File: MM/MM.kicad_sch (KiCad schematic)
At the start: 51 parts, among them J1 USB_C_Receptacle_PowerOnly_6P, J2 Conn_02x16_Odd_Even, SW1 C2890358, SW2 C2890358, U1 DRV8833PWPR, U2 DRV8833PWPR, U3 TP5100, U4 INA219AxD, U5 XL1509-3.3, U6 IP2721, U7 TPS2042D, U8 XL1509-5.0

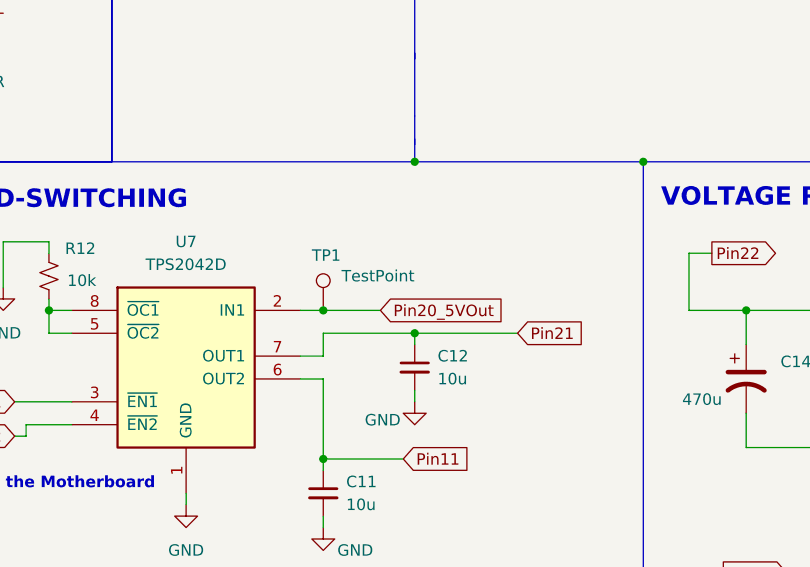
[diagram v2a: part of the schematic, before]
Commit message: Updated voltage regulation, INA219, USB-C, and load-switching circuits. Added verified footprints for 470uF SMD capacitor (C_Elec_8x10.2), IP2721, TPS2042D, and XL1509 regulators. Verified component dimensions and corrected capacitor footprints for JLCPCB compatibility.
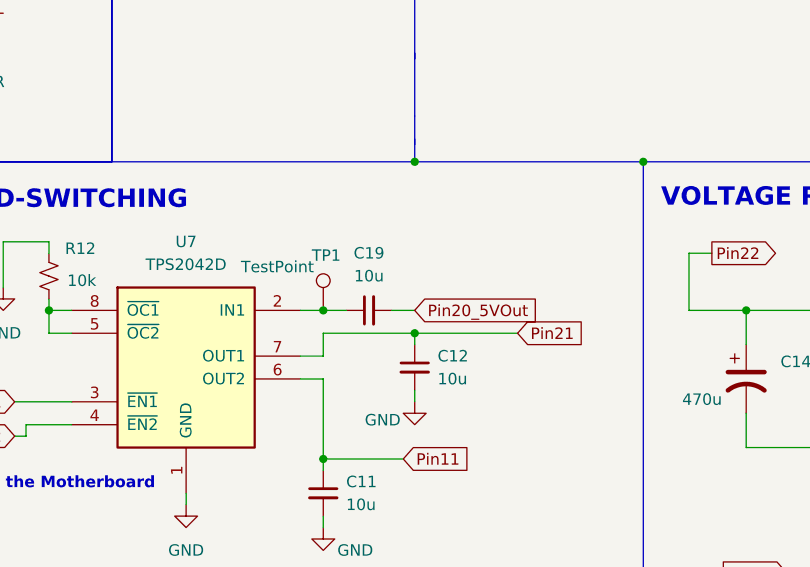
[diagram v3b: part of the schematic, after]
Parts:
- added C19: 10u, CL21A106KAYNNNE:CAPC2012X135N, symbol Device:C_Small
- C10, C11, C12, C9: footprint (none) -> CL21A106KAYNNNE:CAPC2012X135N; LSCS (none) -> C15850
- C14, C16: footprint (none) -> Capacitor_SMD:C_Elec_8x10.2; LSCS (none) -> C3341
- C7, C8: footprint (none) -> CL31B105KBHNNNE:CAPC3216X180N; LSCS (none) -> C1848
- L2: LSCS (none) -> C3341
- R10, R11: footprint (none) -> 0603WAF3301T5E:RESC1608X55N; LSCS (none) -> C22978
- R12, R3, R9: footprint (none) -> 0603WAF1002T5E:RESC1608X55N; LSCS (none) -> C25804
- R5: footprint (none) -> WSL25121L000FEA18:RES_WSL25121L000FEA18; LSCS (none) -> C149567
- R8: footprint (none) -> 0805W8F2003T5E:RESC2012X65N
- U4: footprint Package_SO:SOIC-8_3.9x4.9mm_P1.27mm -> INA219BIDR:SOIC127P599X175-8N
- U7: footprint Package_SO:SOIC-8_3.9x4.9mm_P1.27mm -> TPS2066DR:SOIC127P599X175-8N
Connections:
- net Pin20_5VOut: now also C19.2; no longer TP1.1, U7.2 (IN1)
- new net: C19.1, TP1.1, U7.2 (IN1)

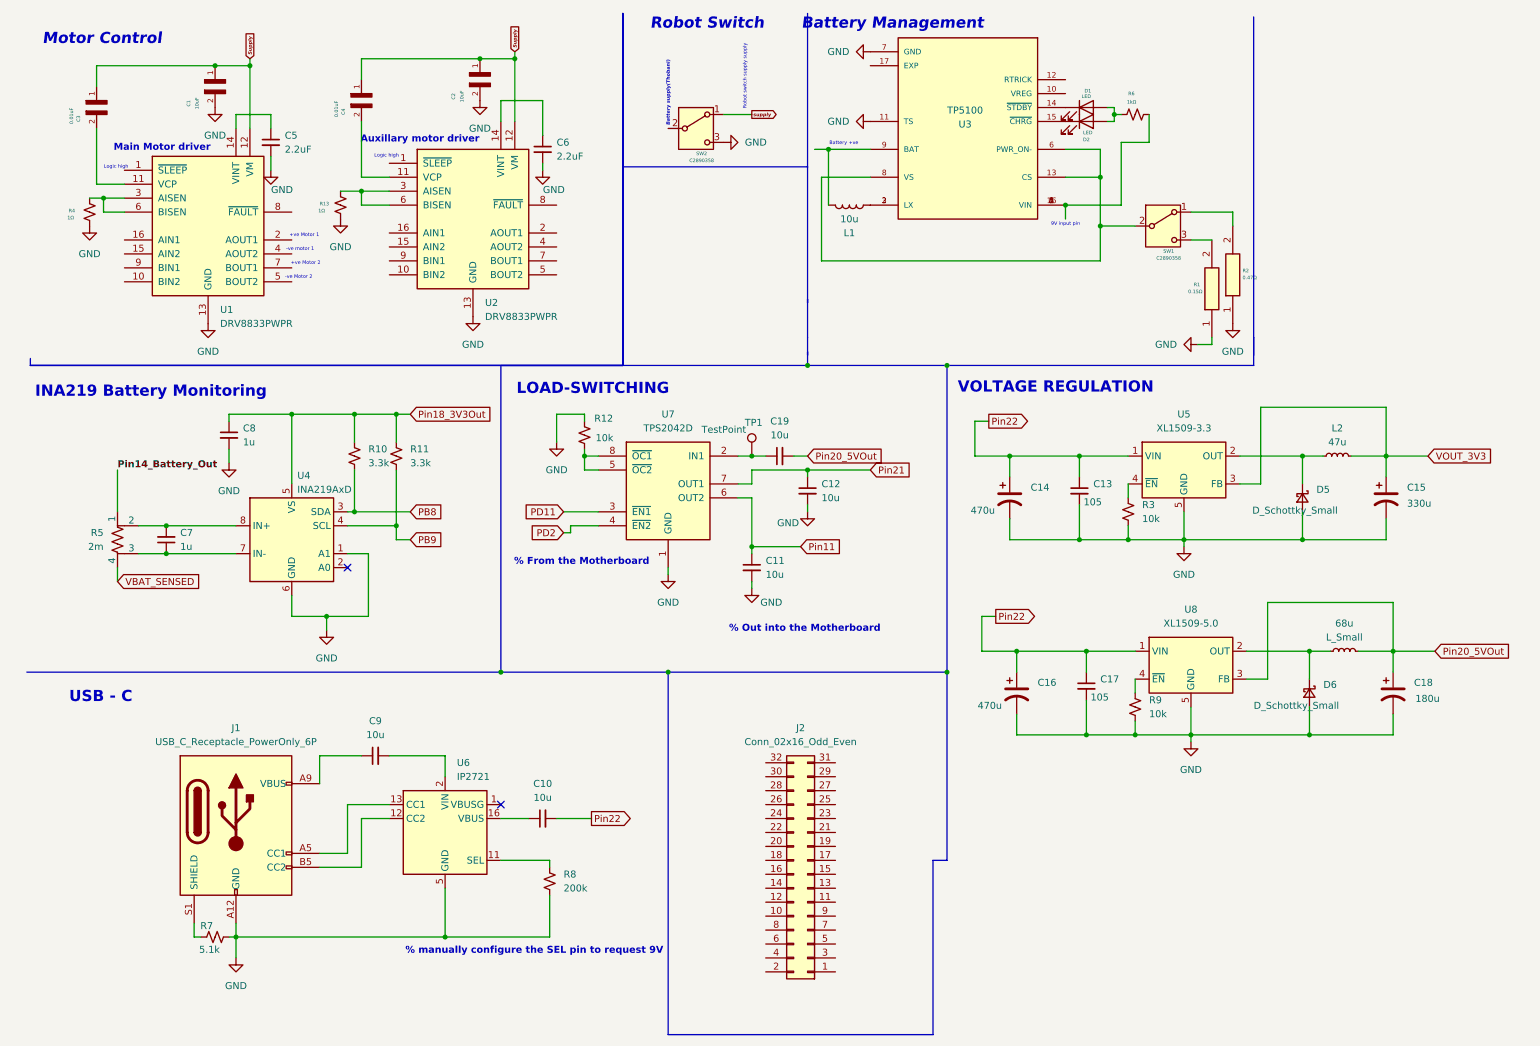
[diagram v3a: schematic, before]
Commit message: Some pins and battery added
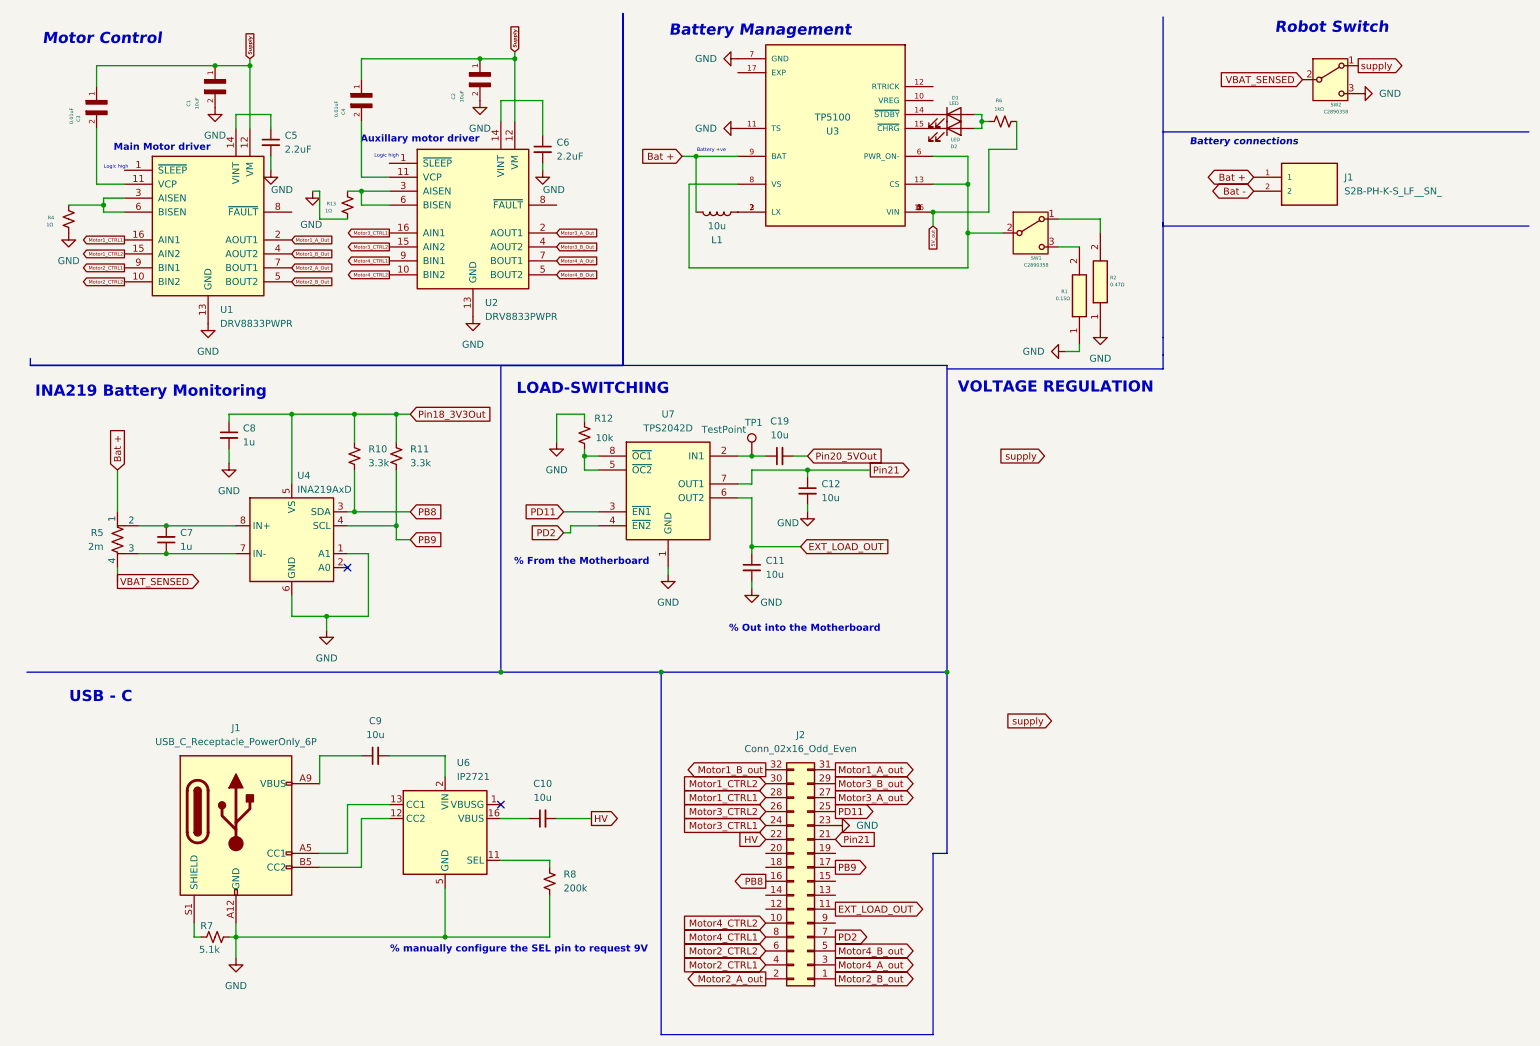
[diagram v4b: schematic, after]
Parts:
- removed 68u: L_Small, symbol Device:L_Small
- removed C13, C17: 105, symbol Device:C_Small
- removed C14, C16: 470u, Capacitor_SMD:C_Elec_8x10.2, symbol Device:C_Polarized_US
- removed C15: 330u, symbol Device:C_Polarized_US
- removed C18: 180u, symbol Device:C_Polarized_US
- removed D5, D6: D_Schottky_Small, symbol Device:D_Schottky_Small
- removed L2: 47u, symbol Device:L_Small
- removed R3, R9: 10k, 0603WAF1002T5E:RESC1608X55N, symbol Device:R_Small_US
- removed U5: XL1509-3.3, Package_SO:SOIC-8_3.9x4.9mm_P1.27mm, symbol Regulator_Switching:XL1509-3.3
- removed U8: XL1509-5.0, Package_SO:SOIC-8_3.9x4.9mm_P1.27mm, symbol Regulator_Switching:XL1509-5.0
- added J1: S2B-PH-K-S_LF__SN_, S2B-PH-K-S_LF__SN_:JST_S2B-PH-K-S_LF__SN_, symbol S2B-PH-K-S_LF__SN_:S2B-PH-K-S_LF__SN_
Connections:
- net Pin11 is gone; now on net EXT_LOAD_OUT: C11.1, U7.6 (OUT2)
- net Pin14_Battery_Out is gone; now on net Bat +: R5.1
- net Pin22 is gone; now on net HV: C10.2
- net GND: now also J2.23 (Pin_23)
- net PB8: now also J2.16 (Pin_16)
- net PB9: now also J2.17 (Pin_17)
- net PD11: now also J2.25 (Pin_25)
- net PD2 : now also J2.7 (Pin_7)
- net Pin21: now also J2.21 (Pin_21)
- net VBAT_SENSED: now also SW2.2 (B)
- net 5V_out: now reaches R6.1, U3.1 (VIN), U3.16 (VIN), U3.4 (VIN), U3.5 (VIN)
- net Bat +: now reaches L1.2, U3.9 (BAT)
- net Bat +: now also J1.1
- net Motor4_CTRL2: now reaches U2.10 (BIN2)
- net Motor4_CTRL2: now also J2.10 (Pin_10)
- net Motor3_CTRL2: now reaches U2.15 (AIN2)
- net Motor3_CTRL2: now also J2.26 (Pin_26)
- net Motor3_CTRL1: now reaches U2.16 (AIN1)
- net Motor3_CTRL1: now also J2.24 (Pin_24)
- net Motor3_A_Out: now reaches U2.2 (AOUT1)
- net Motor3_B_Out: now reaches U2.4 (AOUT2)
- net Motor4_B_Out: now reaches U2.5 (BOUT2)
- net Motor4_A_Out: now reaches U2.7 (BOUT1)
- net Motor4_CTRL1: now reaches U2.9 (BIN1)
- net Motor4_CTRL1: now also J2.8 (Pin_8)
- net Motor2_B_out: now reaches J2.1 (Pin_1)
- net EXT_LOAD_OUT: now reaches J2.11 (Pin_11)
- net Motor2_A_out: now reaches J2.2 (Pin_2)
- net HV: now reaches J2.22 (Pin_22)
- net Motor3_A_out: now reaches J2.27 (Pin_27)
- net Motor1_CTRL1: now reaches J2.28 (Pin_28)
- net Motor1_CTRL1: now also U1.16 (AIN1)
- net Motor3_B_out: now reaches J2.29 (Pin_29)
- net Motor4_A_out: now reaches J2.3 (Pin_3)
- net Motor1_CTRL2: now reaches J2.30 (Pin_30)
- net Motor1_CTRL2: now also U1.15 (AIN2)
- net Motor1_A_out: now reaches J2.31 (Pin_31)
- net Motor1_B_out: now reaches J2.32 (Pin_32)
- net Motor2_CTRL1: now reaches J2.4 (Pin_4)
- net Motor2_CTRL1: now also U1.9 (BIN1)
- net Motor4_B_out: now reaches J2.5 (Pin_5)
- net Motor2_CTRL2: now reaches J2.6 (Pin_6)
- net Motor2_CTRL2: now also U1.10 (BIN2)
- net Motor1_A_Out: now reaches U1.2 (AOUT1)
- net Motor1_B_Out: now reaches U1.4 (AOUT2)
- net Motor2_B_Out: now reaches U1.5 (BOUT2)
- net Motor2_A_Out: now reaches U1.7 (BOUT1)
- new net Bat -: J1.2
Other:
- note added: "Battery connections"
- note removed: "+ve Motor 1"
- note removed: "+ve Motor 2"
- note removed: "-ve Motor 2"
- note removed: "-ve motor 1"
- note removed: "9V input pin"
- note removed: "Battery supply(Thobani)"
- note removed: "Robot switch supply supply"
- moved on the sheet: D1, D2, J2, L1, R1, R13, R2, R4, R6, SW1, U3
